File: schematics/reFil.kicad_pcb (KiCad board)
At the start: 2 copper layers, 19 parts, among them CON1 BARREL_JACK, P1 CONN_5X2, P2 CONN_2, P3 CONN_2, P4 CONN_2, U1 7805

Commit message: Better layout
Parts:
- added 1PIN: P***, 1pin, F.Cu at (40.1, 66.0)
- moved D2 40.1 mm to (79.2, 36.1), turned to 180 degrees
- moved R3 32.2 mm to (73.7, 36.1), turned to 180 degrees
- moved D1 26.9 mm to (68.1, 36.1), turned to 180 degrees
- moved DS1 20.2 mm to (56.9, 49.1), turned to 180 degrees
- moved R2 15.9 mm to (62.5, 36.1), turned to 180 degrees
- moved R1 11.5 mm to (60.6, 61.5), turned to 90 degrees
- moved P2 11.3 mm to (56.3, 61.6), turned to 0 degrees
- moved D3 10.8 mm to (51.3, 36.1), turned to 0 degrees
- moved R4 10.6 mm to (56.6, 36.1)
- moved BCD1 9.17 mm to (47.1, 48.6), turned to 270 degrees
- moved P1 6.32 mm to (39.9, 47.4), turned to 90 degrees
- moved REL1 2.17 mm to (81.5, 53.1)
- moved REL2 2.05 mm to (81.5, 69.1)
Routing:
- net MOTOR: track 60.2 -> 84.1 mm
- net HEAT: track 73.9 -> 53.8 mm
- net TEMP: track 17.9 -> 34.2 mm
- net N-0000010: track 25.6 -> 35.5 mm
- net +5V: track 95.5 -> 86.4 mm
- net N-000006: track 10.1 -> 2.52 mm
- net C: track 5.75 -> 2.67 mm
- net B: track 5.75 -> 2.67 mm
- net D: track 5.75 -> 2.67 mm
- net A: track 5.75 -> 2.67 mm
- net N-000007: track 38.0 -> 38.6 mm
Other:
- board outline added: 46 x 43.1 mm
- board text added: "reFil by @_noskill at @_fixme"

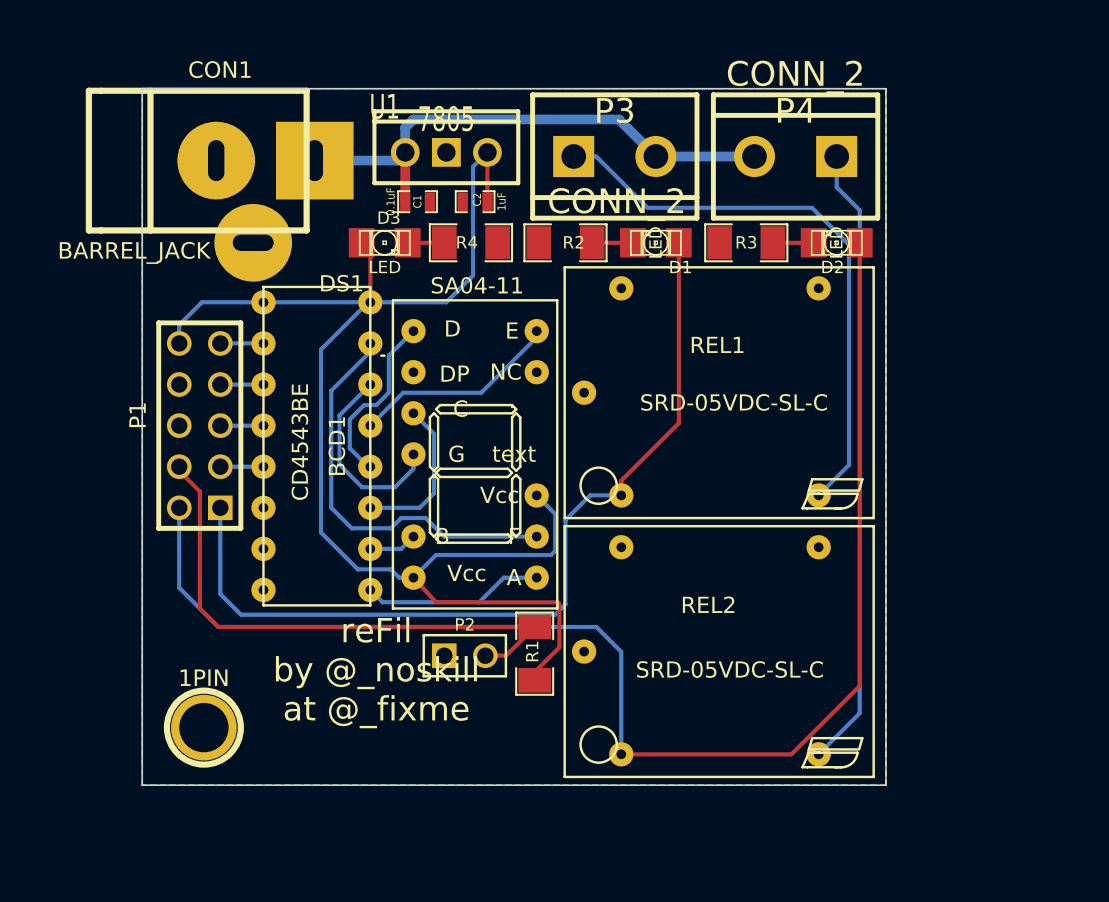
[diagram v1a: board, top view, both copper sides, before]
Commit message: Fix relay footprint pins diameter. Rearrange layout of board for easier mounting.
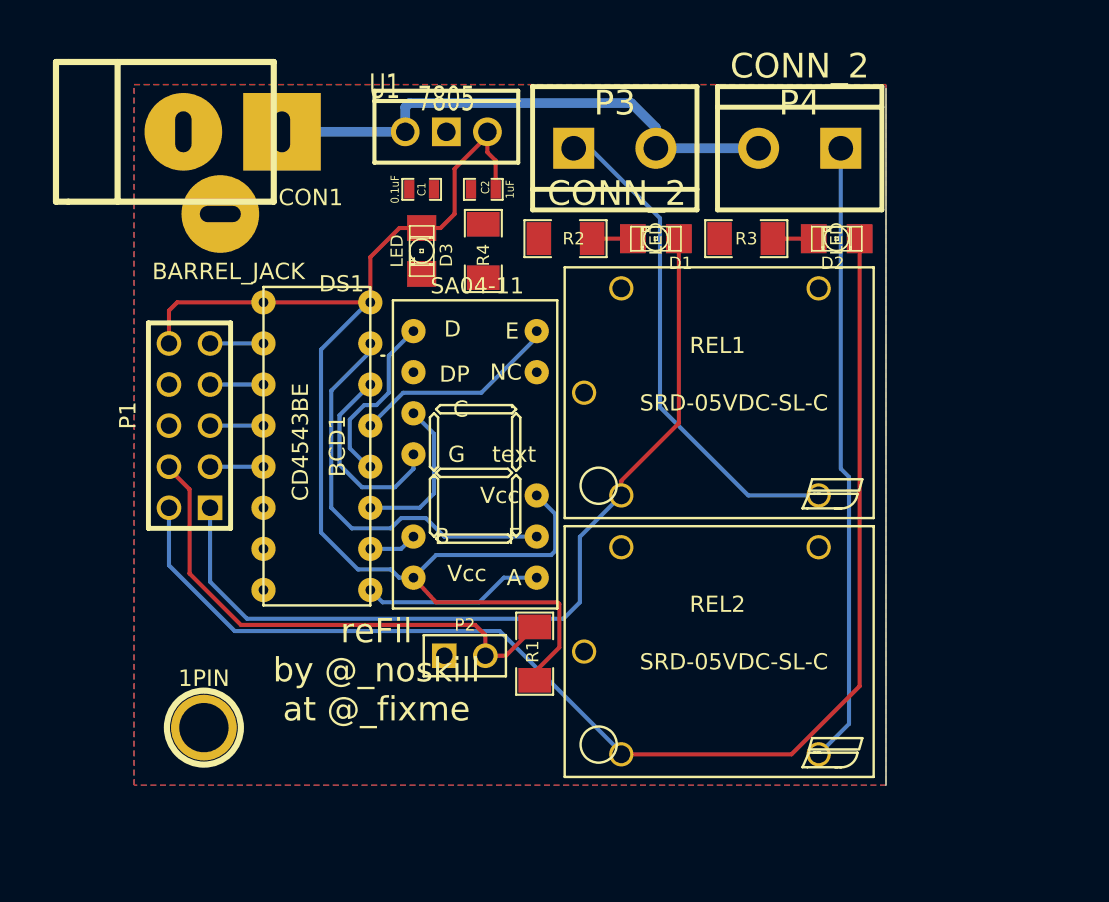
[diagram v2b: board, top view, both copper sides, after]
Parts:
- moved CON1 2.70 mm to (38.9, 29.2)
- moved D3 2.34 mm to (53.6, 36.6), turned to 270 degrees
- moved U1 1.27 mm to (55.1, 29.2)
- moved C2 0.92 mm to (57.4, 32.8)
- moved R4 0.92 mm to (57.4, 36.6), turned to 90 degrees
- moved C1 0.80 mm to (53.6, 32.8)
- moved P1 0.63 mm to (39.2, 47.4)
- moved P4 0.57 mm to (77.0, 30.2)
- moved P3 0.51 mm to (65.5, 30.2)
- moved D1 0.25 mm to (68.1, 35.8)
- moved D2 0.25 mm to (79.2, 35.8)
- moved R2 0.25 mm to (62.5, 35.8)
- moved R3 0.25 mm to (73.7, 35.8)
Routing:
- net N-0000010: track 35.5 -> 30.9 mm
- net MOTOR: track 84.1 -> 80.6 mm
- net N-0000023: track 2.26 -> 0.00 mm
- net TEMP: track 34.2 -> 32.1 mm
- net +5V: track 86.4 -> 84.3 mm
- net D: track 2.67 -> 3.30 mm
- net C: track 2.67 -> 3.30 mm
- net B: track 2.67 -> 3.30 mm
- net A: track 2.67 -> 3.30 mm
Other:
- board outline removed

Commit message: Starting new layout. Better bornier placement.
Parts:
- moved R3 33.5 mm to (85.9, 67.1), turned to 90 degrees
- moved D2 32.7 mm to (88.9, 67.1), turned to 270 degrees
- moved P4 30.5 mm to (87.4, 58.9), turned to 90 degrees
- moved R2 26.9 mm to (84.8, 50.8), turned to 90 degrees
- moved D1 25.2 mm to (88.4, 50.8), turned to 90 degrees
- moved P3 25.1 mm to (87.4, 42.7), turned to 90 degrees
- moved R1 2.64 mm to (58.4, 63.0), turned to 270 degrees
- moved P2 1.73 mm to (55.2, 63.0), turned to 90 degrees
- turned C2 to 0 degrees
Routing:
- net MOTOR: track 80.6 -> 38.4 mm
- net N-000007: track 38.4 -> 0.00 mm
- net N-0000010: track 30.9 -> 0.00 mm
- net TEMP: track 32.1 -> 4.91 mm
- net +24V: track 33.0 -> 11.3 mm
- net +5V: track 84.3 -> 78.1 mm
- net N-000006: track 2.52 -> 0.00 mm
- net N-0000020: track 2.52 -> 0.00 mm
- net HEAT: track 53.8 -> 53.0 mm

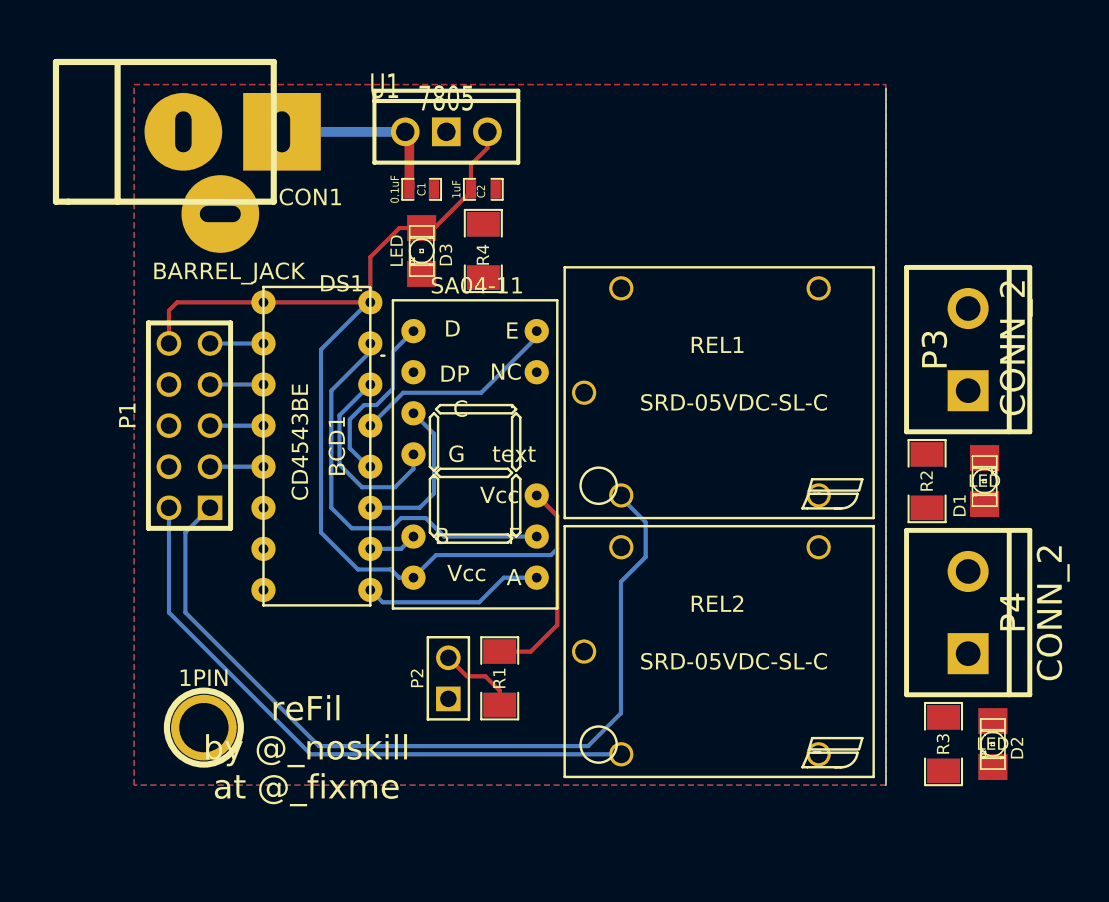
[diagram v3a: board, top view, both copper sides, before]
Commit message: New board layout and gerber export
The 24V connectors (P3, P4) face the opposite side of the barrel jack.
The power LED is now between the barrel jack and the P1 connector
The thermistance connector is now below the temperature display
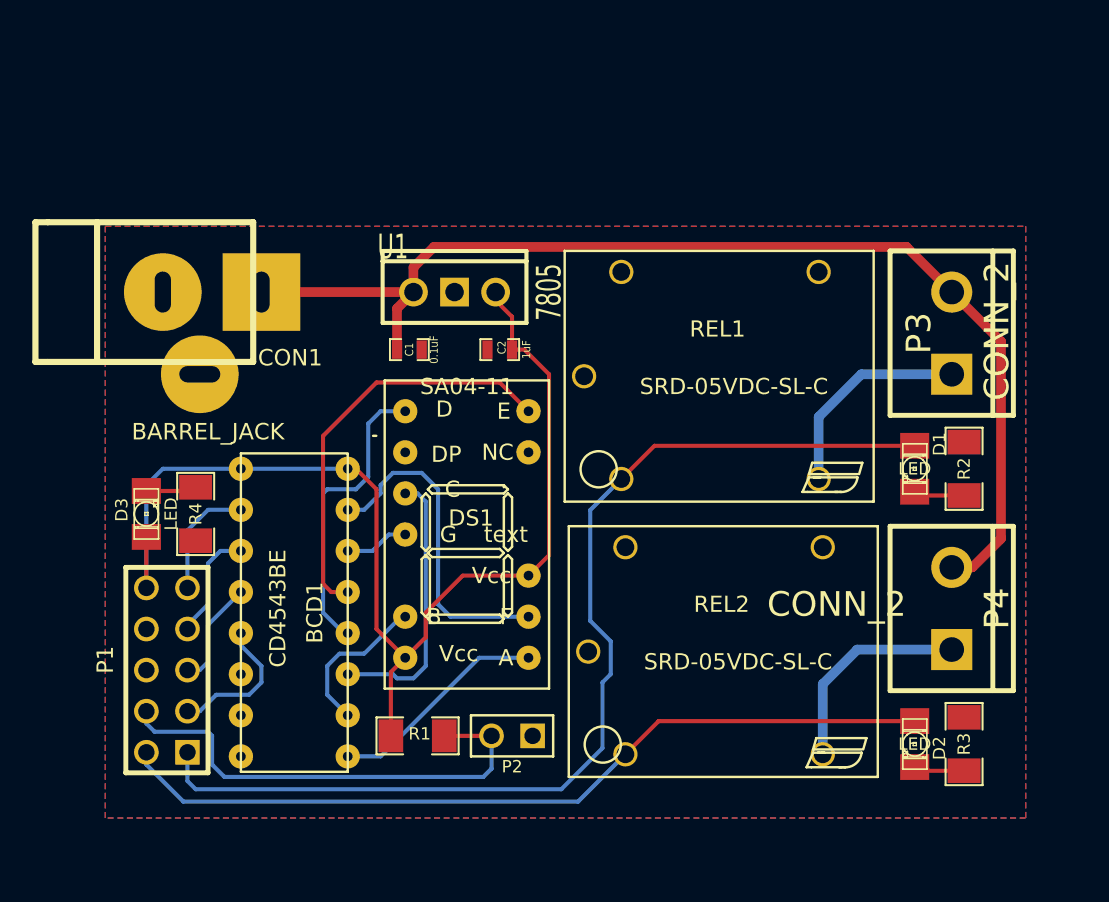
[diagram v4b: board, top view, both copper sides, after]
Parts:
- removed 1PIN: P***, 1pin
- moved R4 24.1 mm to (39.6, 52.8), turned to 270 degrees
- moved D3 23.5 mm to (36.6, 52.8), turned to 90 degrees
- moved P1 15.2 mm to (37.8, 62.5)
- moved BCD1 10.4 mm to (45.7, 58.9)
- moved CON1 9.99 mm to (37.6, 39.1)
- moved C2 9.96 mm to (58.4, 42.7), turned to 180 degrees
- moved C1 9.94 mm to (52.8, 42.7)
- moved U1 9.92 mm to (55.6, 39.1)
- moved R1 6.20 mm to (53.3, 66.5), turned to 0 degrees
- moved P2 5.31 mm to (59.2, 66.5), turned to 180 degrees
- moved DS1 4.98 mm to (56.4, 54.1)
- moved D2 4.83 mm to (84.1, 67.1)
- moved D1 4.38 mm to (84.1, 50.0), turned to 270 degrees
- moved R2 2.41 mm to (87.1, 50.0)
- moved P3 1.44 mm to (86.4, 41.7)
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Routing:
- net +24V: track 11.3 -> 70.1 mm
- net TEMP: track 4.91 -> 29.7 mm
- net N-000007: track 0.00 -> 13.2 mm
- net N-0000010: track 0.00 -> 13.2 mm
- net HEAT: track 53.0 -> 65.9 mm
- net MOTOR: track 38.4 -> 51.3 mm
- net N-0000015: track 12.9 -> 25.7 mm
- net N-0000012: track 12.3 -> 3.98 mm
- net N-0000016: track 11.1 -> 18.5 mm
- net N-0000017: track 9.78 -> 16.9 mm
- net N-0000018: track 2.98 -> 9.66 mm
- net +5V: track 78.1 -> 71.5 mm
- net A: track 3.30 -> 8.88 mm
- net N-0000014: track 25.1 -> 20.3 mm
- net C: track 3.30 -> 7.38 mm
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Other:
- board text removed: "reFil by @_noskill at @_fixme"
